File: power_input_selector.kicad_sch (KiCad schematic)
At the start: 35 parts, among them Q1 SUD50P06-15, Q2 SUD50P06-15, Q3 SUD50P06-15, Q4 SUD50P06-15, Q5 SUD50P06-15, Q6 SUD50P06-15, U1 LTC4417IGN, U7 INA236BIDDFR, U8 INA236BIDDFR

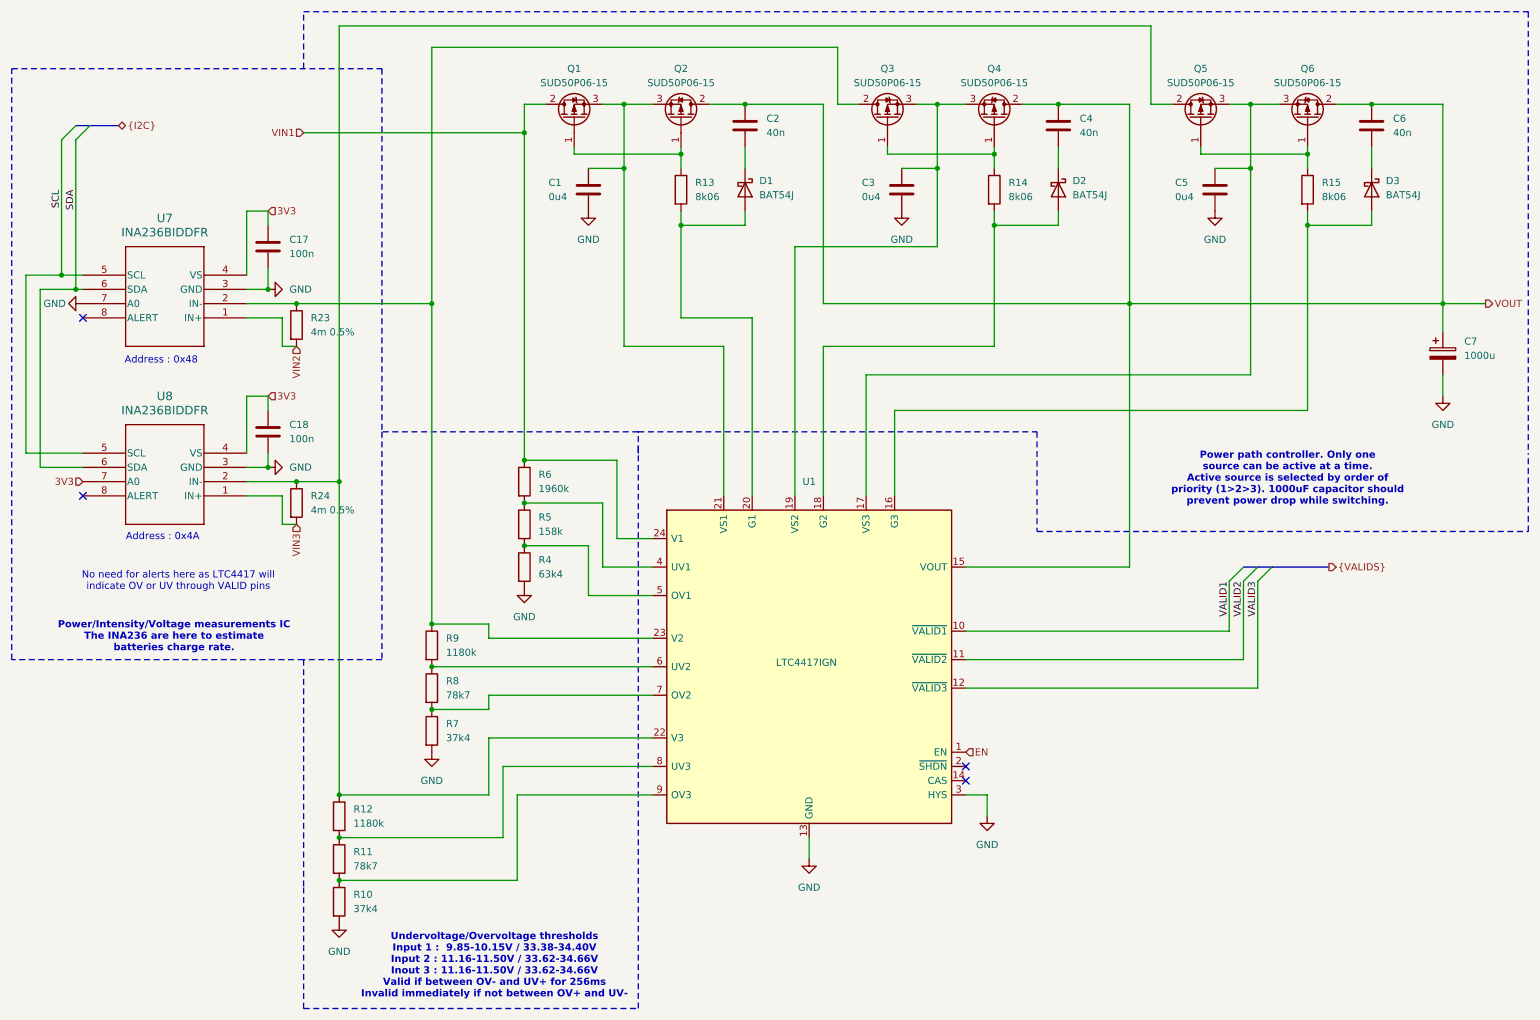
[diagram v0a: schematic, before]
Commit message: Correctifs et améliorations + passage à KiCad V9
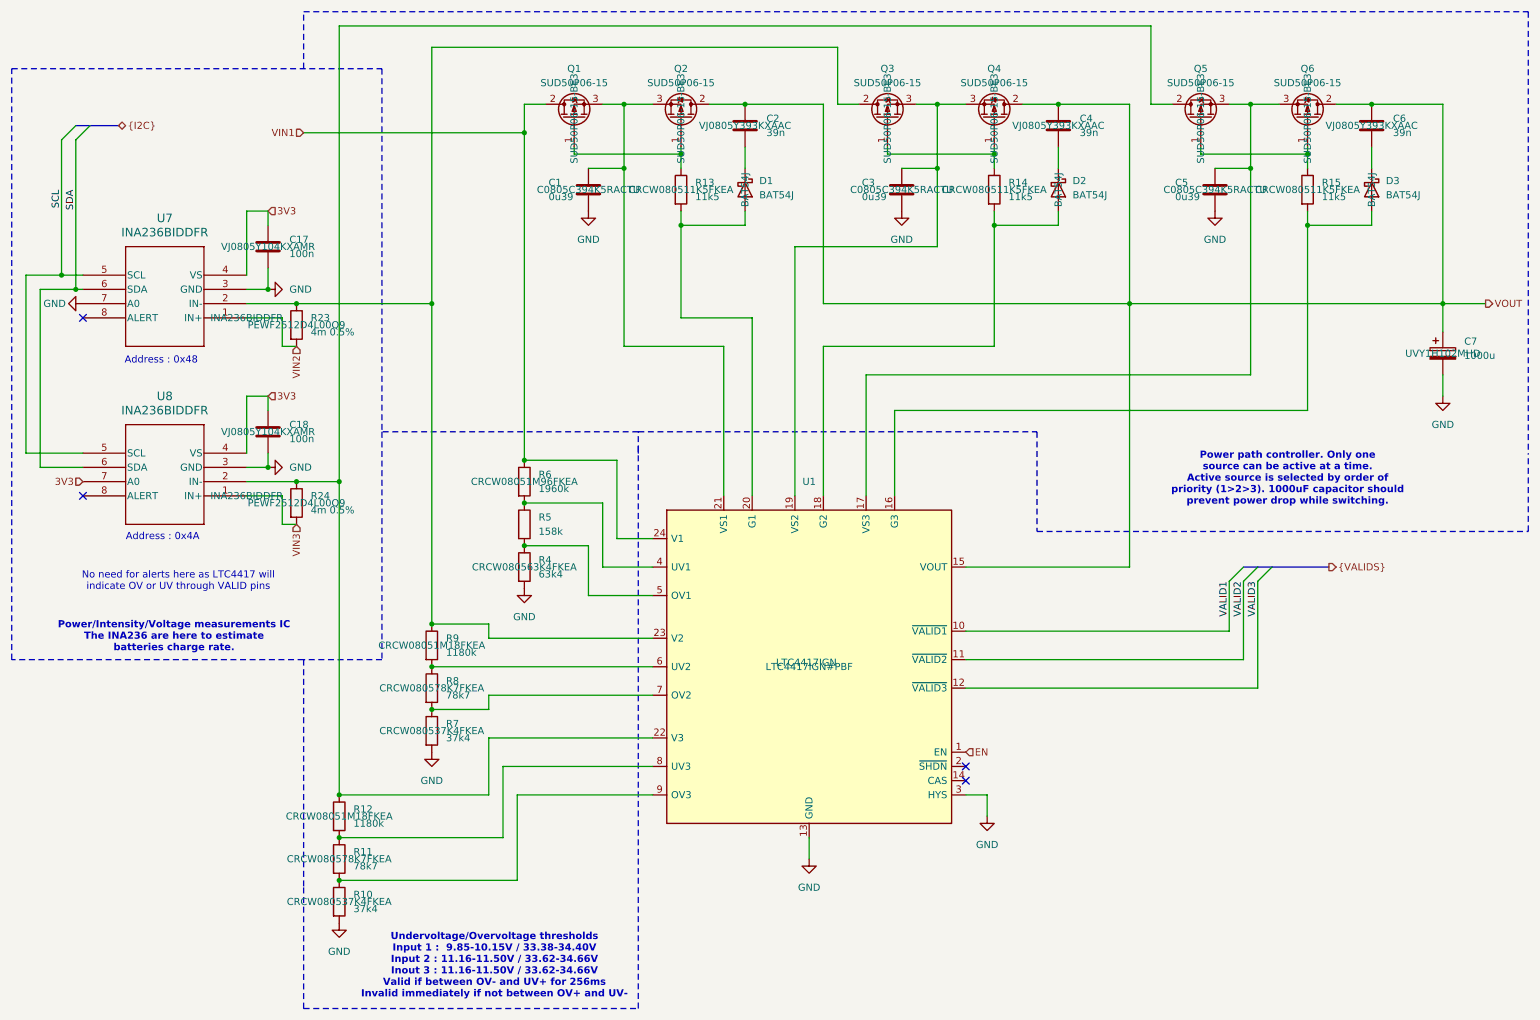
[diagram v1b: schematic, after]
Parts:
- C1, C3, C5: value 0u4 -> 0u39; Manufacturer_Part_Number (none) -> C0805C394K5RACTU
- C17, C18: Manufacturer_Part_Number (none) -> VJ0805Y104KXAMR
- C2, C4, C6: value 40n -> 39n; Manufacturer_Part_Number (none) -> VJ0805Y393KXAAC
- C7: Manufacturer_Part_Number (none) -> UVY1H102MHD
- D1, D2, D3: Manufacturer_Part_Number (none) -> BAT54J
- Q1, Q2, Q3, Q4, Q5, Q6: Manufacturer_Part_Number (none) -> SUD50P06-15-BE3
- R10, R7: Manufacturer_Part_Number (none) -> CRCW080537K4FKEA
- R11, R8: Manufacturer_Part_Number (none) -> CRCW080578K7FKEA
- R12, R9: Manufacturer_Part_Number (none) -> CRCW08051M18FKEA
- R13, R14, R15: value 8k06 -> 11k5; Manufacturer_Part_Number (none) -> CRCW080511K5FKEA
- R23, R24: Manufacturer_Part_Number (none) -> PEWF2512D4L00Q9
- R4: Manufacturer_Part_Number (none) -> CRCW080563K4FKEA
- R6: Manufacturer_Part_Number (none) -> CRCW08051M96FKEA
- U1: Manufacturer_Part_Number (none) -> LTC4417IGN#PBF
- U7, U8: Manufacturer_Part_Number (none) -> INA236BIDDFR
